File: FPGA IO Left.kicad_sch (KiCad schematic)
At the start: 9 parts, among them U1 LFE5UM5G-85F-8BG381x, X1 SG-5032CAN

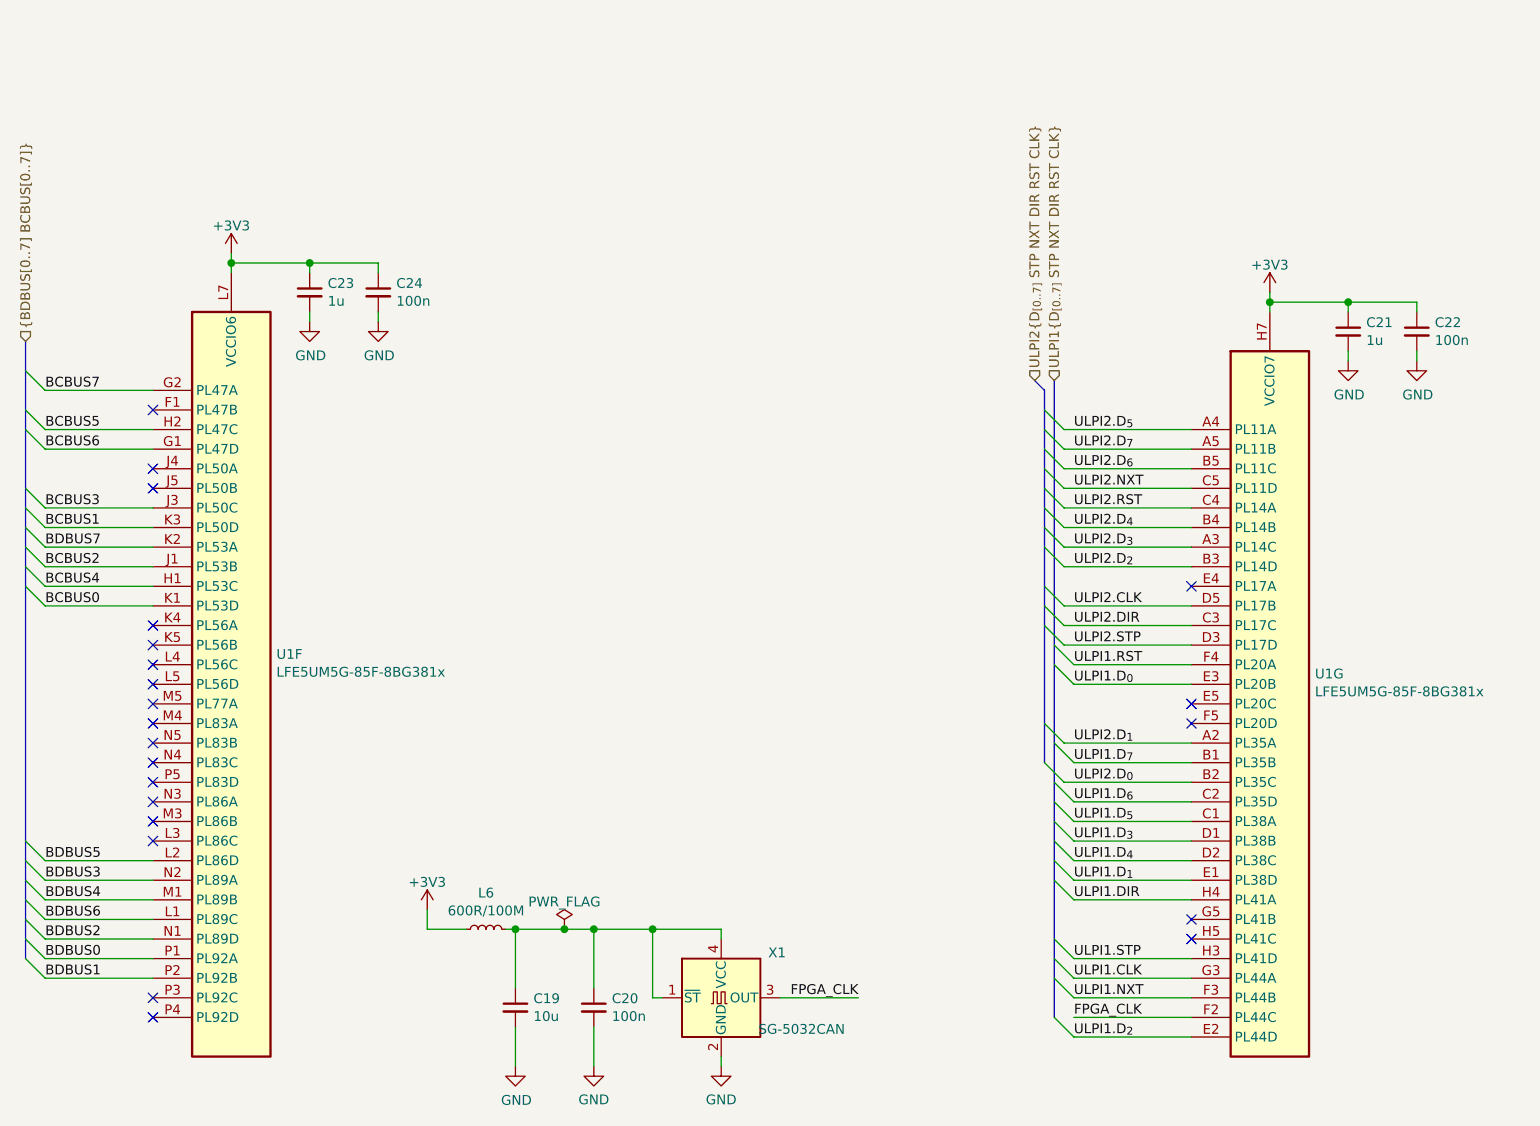
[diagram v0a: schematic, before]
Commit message: Update to KiCad 6
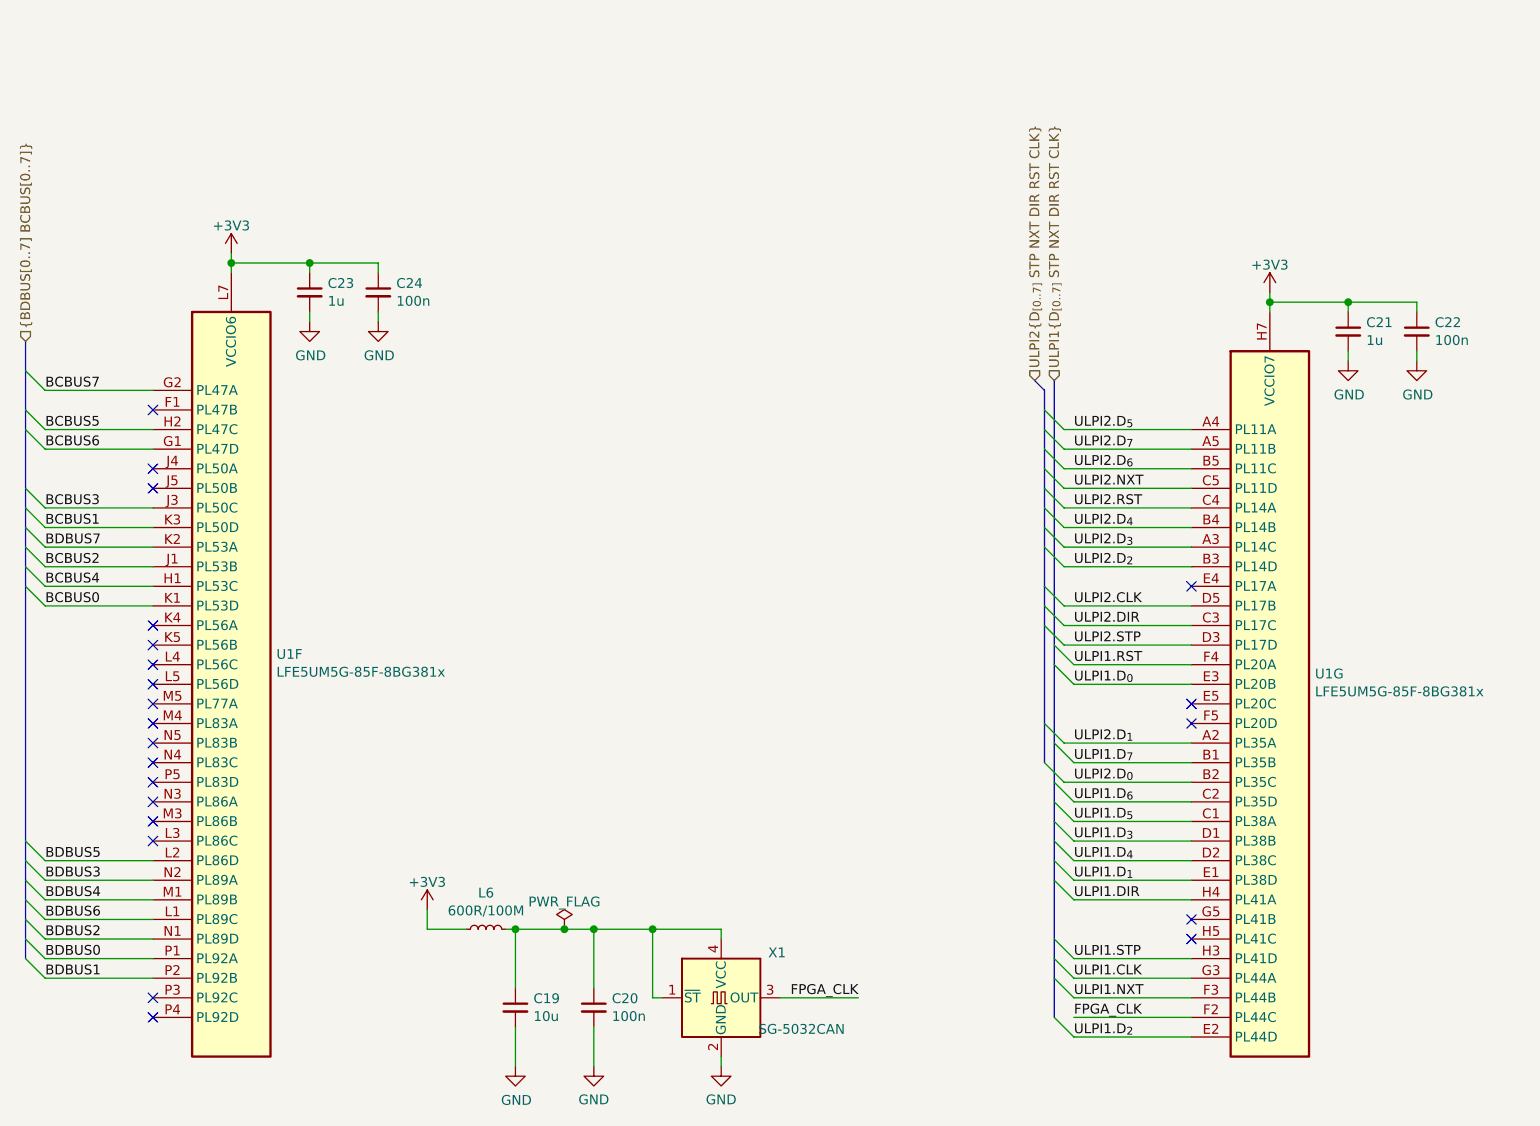
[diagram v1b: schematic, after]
